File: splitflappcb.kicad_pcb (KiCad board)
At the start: 2 copper layers, 40 x 80 mm, 45 parts, among them J1 Conn_01x04_Pin, J2 Conn_01x04_Pin, J3 Conn_01x05_Pin, J4 AddressJumpers, J5 HallSensor, J6 AVR-ISP-6, J7 Serial-328P, J8 Serial-ESP12E, J9 WS2815, SW1 RESET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

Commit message: update to rev1.1
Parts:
- added R8: 10k, Resistor_SMD:R_0402_1005Metric, F.Cu at (86.3, 97.0)
- moved R6 0.41 mm to (91.7, 96.5)
- moved R7 0.41 mm to (89.8, 96.5)
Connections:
- U4 pad 16: unconnected-(U4-GPIO15-Pad16) -> Net-(U4-GPIO15)
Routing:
- net Net-(U4-GPIO15): track 0.00 -> 1.93 mm
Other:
- board text added: "rev 1.1"
- board text removed: "rev 1.0"

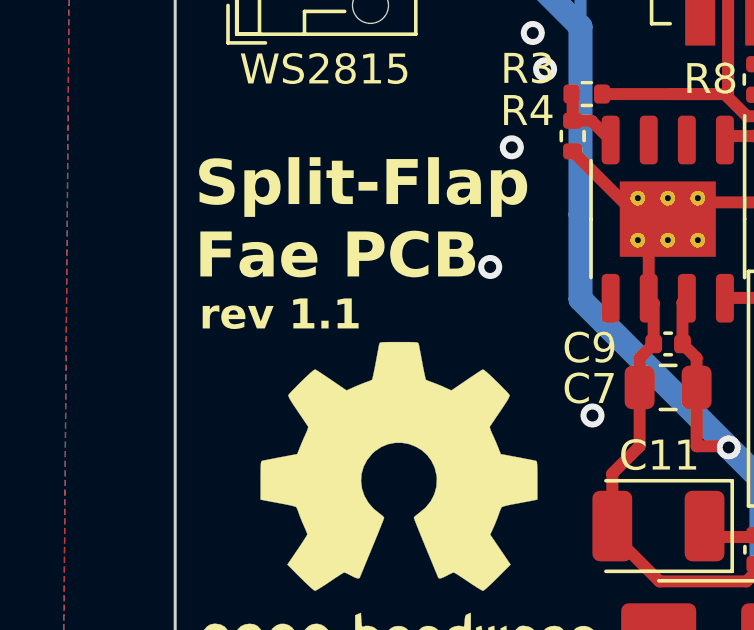
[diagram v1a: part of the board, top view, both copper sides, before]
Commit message: rev 1.2 – fix incorrect pin labels on ISP connector (fixes #1)
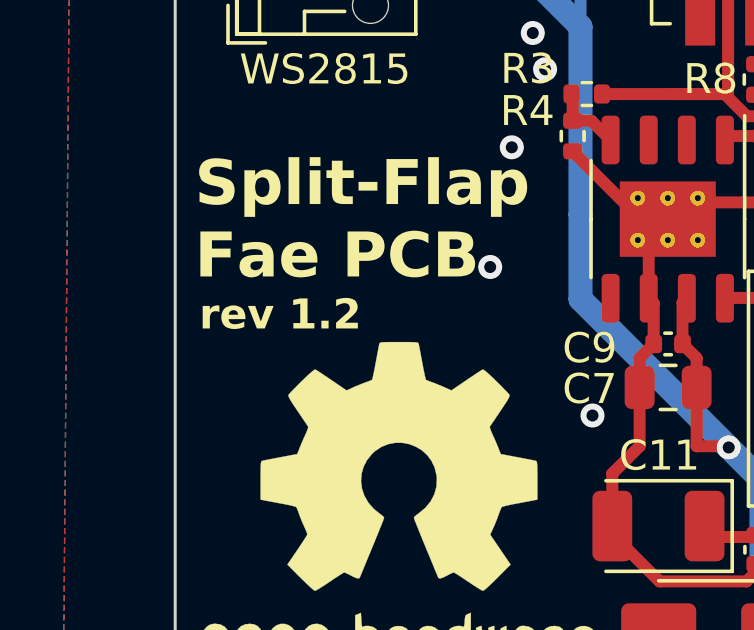
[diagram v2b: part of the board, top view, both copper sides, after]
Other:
- board text added: "rev 1.2"
- board text removed: "rev 1.1"
